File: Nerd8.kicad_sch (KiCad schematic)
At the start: 3 parts, among them J1 Conn_01x04

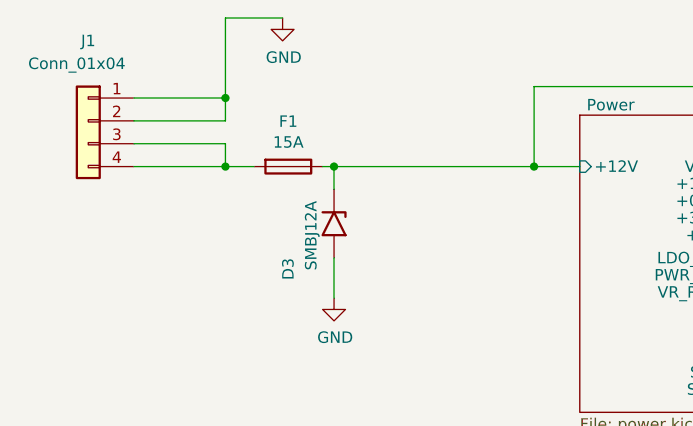
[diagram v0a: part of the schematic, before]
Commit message: Input Cap 12V LED
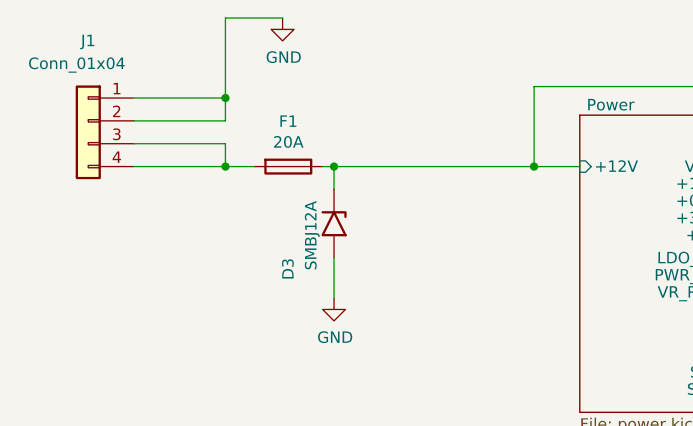
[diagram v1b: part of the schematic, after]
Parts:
- F1: value 15A -> 20A; Manufacturer 0451015.MRL -> 0451020.MRL
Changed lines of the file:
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@@
 			)
 		)
-		(property "Value" "15A"
+		(property "Value" "20A"
 			(at 50.165 49.3776 90)
 			(effects
@@
 			)
 		)
-		(property "Manufacturer" "0451015.MRL"
+		(property "Manufacturer" "0451020.MRL"
 			(at 50.165 52.07 0)
 			(effects

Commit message: BOM partdescriptions
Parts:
- F1: OrderNr F2593CT-ND -> F8251CT-ND
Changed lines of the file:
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@@
 			)
 		)
-		(property "Description" "Generic connector, single row, 01x04, script generated (kicad-library-utils/schlib/autogen/connector/)"
+		(property "Description" "CONN BARRIER STRIP 4CIRC 0.374\""
 			(at 27.94 46.99 0)
 			(effects
@@
 			)
 		)
-		(property "Description" ""
+		(property "Description" "TVS DIODE 12VWM 19.9VC DO214AA"
 			(at 55.245 58.42 0)
 			(effects
@@
 			)
 		)
-		(property "Description" ""
+		(property "Description" "FUSE BRD MNT 20A 65VAC 65VDC SMD"
 			(at 50.165 52.07 0)
 			(effects
@@
 			)
 		)
-		(property "OrderNr" "F2593CT-ND"
-			(at 50.165 52.07 0)
-			(effects
+		(property "OrderNr" "F8251CT-ND"
+			(at 50.165 52.07 0)
+			(effects
